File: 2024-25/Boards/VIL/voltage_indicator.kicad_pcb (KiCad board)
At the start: 2 copper layers, 38.1 x 49.9 mm, 10 parts, among them Q1 VN2460, Q2 UJ3N120035K3S

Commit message: checkbox schm
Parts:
- added H1: MountingHole, MountingHole:MountingHole_4.3mm_M4, F.Cu at (120.2, 66.4)
- added H2: MountingHole, MountingHole:MountingHole_4.3mm_M4, F.Cu at (156.2, 66.6)
- added H3: MountingHole, MountingHole:MountingHole_4.3mm_M4, F.Cu at (120.2, 107.6)
- added H4: MountingHole, MountingHole:MountingHole_4.3mm_M4, F.Cu at (156.2, 107.6)
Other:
- board size 38.1 x 49.9 mm -> 47.1 x 53.3 mm

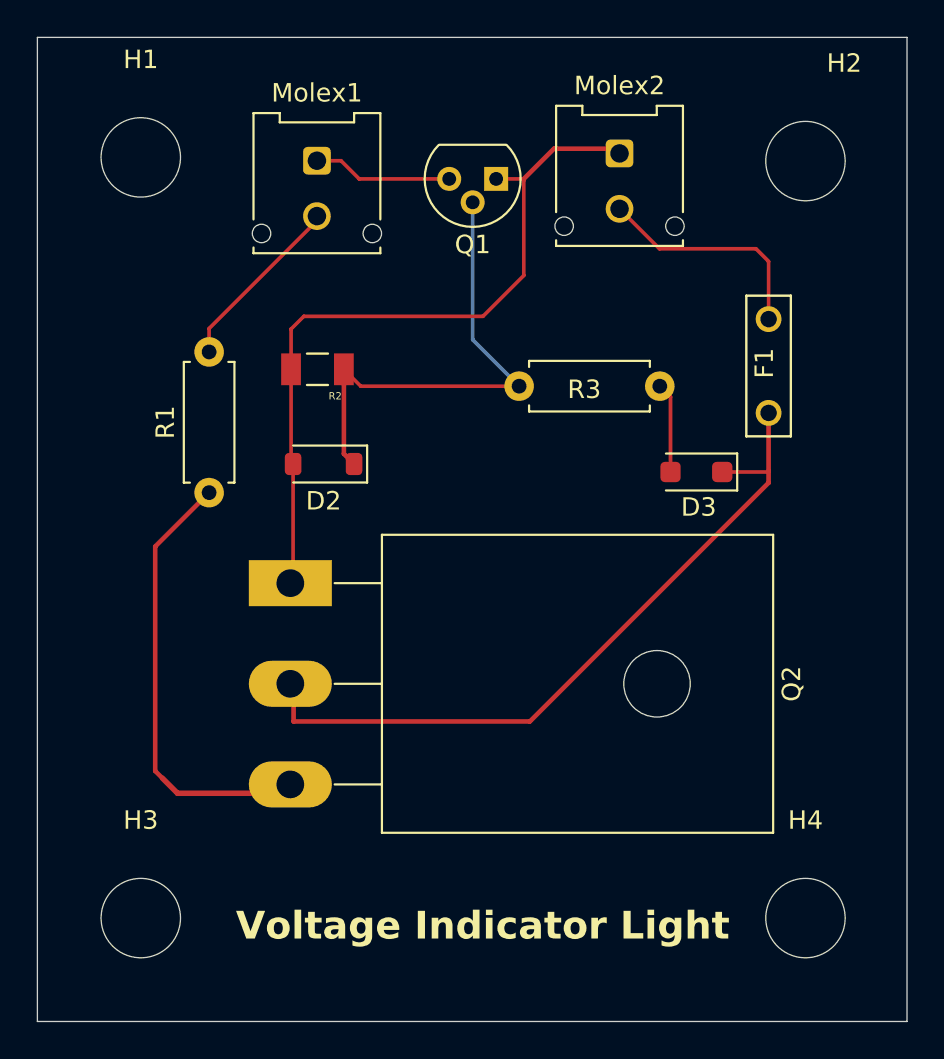
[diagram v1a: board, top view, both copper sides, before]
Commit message: updated voltage indicator to v1.1
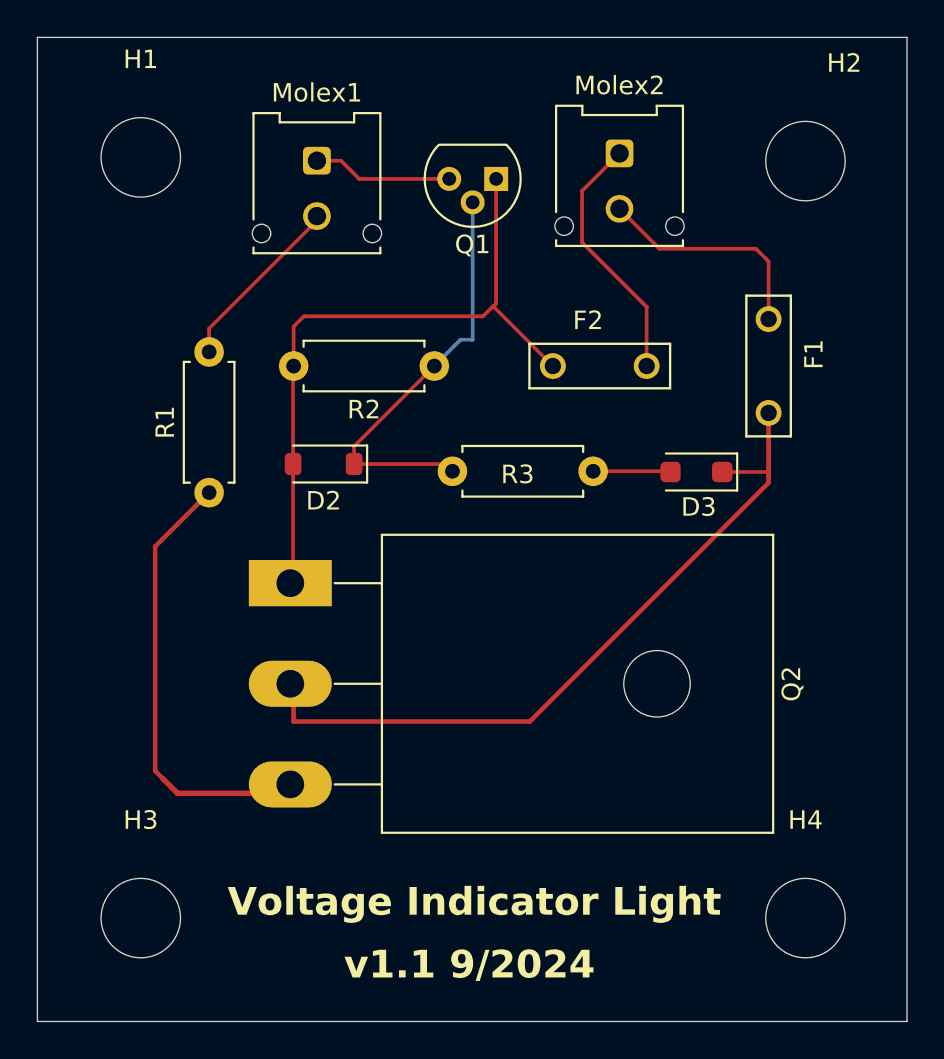
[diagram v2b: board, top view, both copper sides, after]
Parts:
- added F2: 750mA, Library:FUSE_BK_PCS, F.Cu at (145.1, 77.7)
- F1: footprint BK_PCS:FUSE_BK_PCS -> Library:FUSE_BK_PCS
- Q2: value UJ3N120035K3S -> UJ3N065080K3S
- R2: value RK73G2BTTD1004C -> 1M; footprint Resistor_SMD:RESC3116X65N -> Resistor_THT:R_Axial_DIN0207_L6.3mm_D2.5mm_P7.62mm_Horizontal
- moved R2 6.33 mm to (136.1, 77.7)
- moved R3 5.86 mm to (144.7, 83.4)
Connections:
- net Net-(D3-K) renamed /HV+_fused
- D2 pad 2: /HV- -> /HV-_fused
- Q1 pad 1: /HV- -> /HV-_fused
- Q2 pad 1: /HV- -> /HV-_fused
- R2 pad 2: /HV- -> /HV-_fused
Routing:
- net /HV-_fused: track 0.00 -> 37.0 mm
- net /HV-: track 40.4 -> 14.2 mm
- net Net-(D2-K): track 26.2 -> 22.7 mm
- net Net-(D3-A): track 4.89 -> 4.21 mm
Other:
- board text added: "v1.1 9/2024"

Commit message: updated resistors to be smd on VIL and added fuses and mounting holes to TSAL
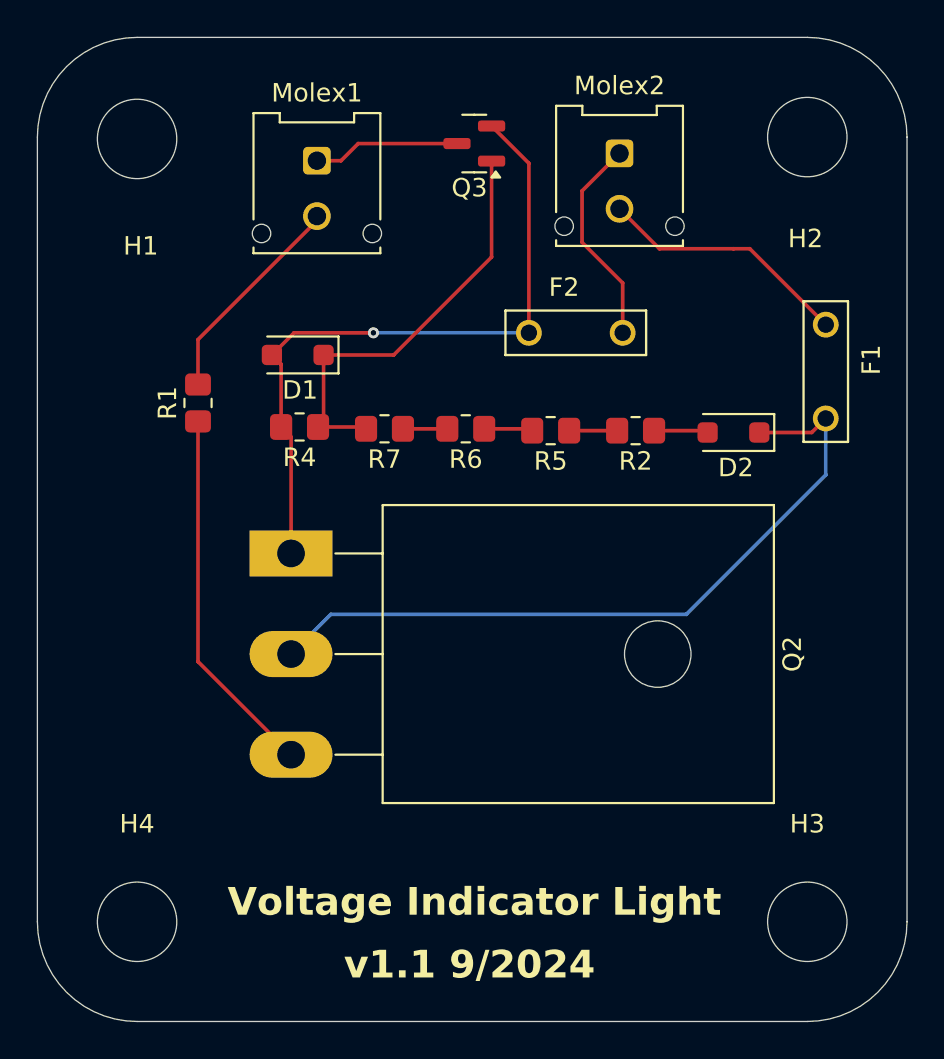
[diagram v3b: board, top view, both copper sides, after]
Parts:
- removed D3: PZ1AL62B-AU_R1_000A1, Diode_SMD:D_SOD-123F
- removed Q1: VN2460, Package_TO_SOT_THT:TO-92
- removed R3: PR02000201004FA100, Resistor_THT:R_Axial_DIN0207_L6.3mm_D2.5mm_P7.62mm_Horizontal
- added D1: BZT52C12, Diode_SMD:D_SOD-123F, F.Cu at (128.7, 77.1)
- added Q3: DMN2056U, Package_TO_SOT_SMD:SOT-23, F.Cu at (138.3, 65.7)
- added R4: 2M, Resistor_SMD:R_0805_2012Metric_Pad1.20x1.40mm_HandSolder, F.Cu at (128.8, 81.0)
- added R5: 250k, Resistor_SMD:R_0805_2012Metric_Pad1.20x1.40mm_HandSolder, F.Cu at (142.4, 81.2)
- added R6: 250k, Resistor_SMD:R_0805_2012Metric_Pad1.20x1.40mm_HandSolder, F.Cu at (137.8, 81.1)
- added R7: 250k, Resistor_SMD:R_0805_2012Metric_Pad1.20x1.40mm_HandSolder, F.Cu at (133.4, 81.1)
- D2: value BZT52-B12_R1_00001 -> BZT52C51; footprint Diode_SMD:D_SOD-123 -> Diode_SMD:D_SOD-123F
- R1: footprint Resistor_THT:R_Axial_DIN0207_L6.3mm_D2.5mm_P7.62mm_Horizontal -> Resistor_SMD:R_0805_2012Metric_Pad1.20x1.40mm_HandSolder
- R2: value 1M -> 250k; footprint Resistor_THT:R_Axial_DIN0207_L6.3mm_D2.5mm_P7.62mm_Horizontal -> Resistor_SMD:R_0805_2012Metric_Pad1.20x1.40mm_HandSolder
- moved H4 36.2 mm to (120.0, 107.8)
- moved H3 36.1 mm to (156.3, 107.8)
- moved D2 22.3 mm to (152.3, 81.3)
- moved R2 11.4 mm to (147.0, 81.2)
- moved R1 4.89 mm to (123.3, 79.7)
- moved F1 3.11 mm to (157.3, 78.0)
- moved F2 2.22 mm to (143.8, 75.9)
- moved Q2 1.61 mm to (128.3, 87.8)
- moved H2 1.30 mm to (156.3, 65.3)
- moved H1 1.02 mm to (120.0, 65.4)
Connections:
- D2 pad 1: Net-(D2-K) -> /HV+_fused
- D2 pad 2: /HV-_fused -> Net-(D2-A)
- R2 pad 1: Net-(D2-K) -> Net-(D2-A)
- R2 pad 2: /HV-_fused -> Net-(R2-Pad2)
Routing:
- net Net-(D1-K): track 0.00 -> 23.2 mm
- net Net-(D2-K): track 22.7 -> 0.00 mm
- net Net-(D3-A): track 4.21 -> 0.00 mm
- net Net-(Q2-S): track 24.3 -> 20.1 mm
- net Net-(D2-A): track 0.00 -> 2.94 mm
- net Net-(R5-Pad2): track 0.00 -> 2.64 mm
- net Net-(R2-Pad2): track 0.00 -> 2.60 mm
- net Net-(R6-Pad2): track 0.00 -> 2.40 mm
- net /HV-: track 14.2 -> 11.8 mm
- net /LED+: track 9.75 -> 11.8 mm
- net /HV+: track 12.4 -> 13.8 mm
- net /HV-_fused: track 37.0 -> 37.6 mm, vias 0 -> 1
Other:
- outline, holes or cut-outs redrawn

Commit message: fixed up part names and added dnps
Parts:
- R2, R5, R6, R7: value 250k -> 240k
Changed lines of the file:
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@@
 		(sheetname "Root")
 		(sheetfile "voltage_indicator.kicad_sch")
-		(attr through_hole)
+		(attr through_hole dnp)
 		(fp_line
 			(start -3.435 -2.58)
@@
 		(tags "resistor handsolder")
 		(property "Reference" "R6"
-			(at 0 -1.65 360)
+			(at 0 -1.65 0)
 			(layer "F.SilkS")
 			(effects
@@
 			)
 		)
-		(property "Value" "250k"
-			(at 0 1.65 360)
+		(property "Value" "240k"
+			(at 0 1.65 0)
 			(layer "F.Fab")
 			(effects
@@
 		)
 		(fp_text user "${REFERENCE}"
-			(at 0 0 360)
+			(at 0 0 0)
 			(layer "F.Fab")
 			(effects
@@
 		(tags "resistor handsolder")
 		(property "Reference" "R4"
-			(at 0 -1.65 360)
+			(at 0 -1.65 0)
 			(layer "F.SilkS")
 			(effects
@@
 		)
 		(property "Value" "2M"
-			(at 0 1.65 360)
+			(at 0 1.65 0)
 			(layer "F.Fab")
 			(effects
@@
 		)
 		(fp_text user "${REFERENCE}"
-			(at 0 0 360)
+			(at 0 0 0)
 			(layer "F.Fab")
 			(effects
@@
 		(sheetname "Root")
 		(sheetfile "voltage_indicator.kicad_sch")
-		(attr through_hole)
+		(attr through_hole dnp)
 		(fp_line
 			(start -3.435 -2.58)
@@
 		(tags "resistor handsolder")
 		(property "Reference" "R5"
-			(at 0 -1.65 360)
+			(at 0 -1.65 0)
 			(layer "F.SilkS")
 			(effects
@@
 			)
 		)
-		(property "Value" "250k"
-			(at 0 1.65 360)
+		(property "Value" "240k"
+			(at 0 1.65 0)
 			(layer "F.Fab")
 			(effects
@@
 		)
 		(fp_text user "${REFERENCE}"
-			(at 0 0 360)
+			(at 0 0 0)
 			(layer "F.Fab")
 			(effects
@@
 		(tags "D_SOD-123F")
 		(property "Reference" "D1"
-			(at -0.127 -1.905 360)
+			(at -0.127 -1.905 0)
 			(layer "F.SilkS")
 			(effects
@@
 		)
 		(property "Value" "BZT52C12"
-			(at 0 2.1 360)
+			(at 0 2.1 0)
 			(layer "F.Fab")
 			(effects
@@
 		)
 		(fp_text user "${REFERENCE}"
-			(at -0.127 -1.905 360)
+			(at -0.127 -1.905 0)
 			(layer "F.Fab")
 			(effects
@@
 		(tags "resistor handsolder")
 		(property "Reference" "R7"
-			(at 0 -1.65 360)
+			(at 0 -1.65 0)
 			(layer "F.SilkS")
 			(effects
@@
 			)
 		)
-		(property "Value" "250k"
-			(at 0 1.65 360)
+		(property "Value" "240k"
+			(at 0 1.65 0)
 			(layer "F.Fab")
 			(effects
@@
 		)
 		(fp_text user "${REFERENCE}"
-			(at 0 0 360)
+			(at 0 0 0)
 			(layer "F.Fab")
 			(effects
@@
 		(tags "resistor handsolder")
 		(property "Reference" "R2"
-			(at 0 -1.65 360)
+			(at 0 -1.65 0)
 			(layer "F.SilkS")
 			(effects
@@
 			)
 		)
-		(property "Value" "250k"
-			(at 0 1.65 360)
+		(property "Value" "240k"
+			(at 0 1.65 0)
 			(layer "F.Fab")
 			(effects
@@
 		)
 		(fp_text user "${REFERENCE}"
-			(at 0 0 360)
+			(at 0 0 0)
 			(layer "F.Fab")
 			(effects
@@
 		(sheetname "Root")
 		(sheetfile "voltage_indicator.kicad_sch")
-		(attr through_hole)
+		(attr through_hole dnp)
 		(fp_line
 			(start -2.62 -4.96)
@@
 		(sheetname "Root")
 		(sheetfile "voltage_indicator.kicad_sch")
-		(attr through_hole)
+		(attr through_hole dnp)
 		(fp_line
 			(start -3.81 -1.205)
@@
 		(sheetname "Root")
 		(sheetfile "voltage_indicator.kicad_sch")
-		(attr through_hole)
+		(attr through_hole dnp)
 		(fp_line
 			(start -3.81 1.205)
